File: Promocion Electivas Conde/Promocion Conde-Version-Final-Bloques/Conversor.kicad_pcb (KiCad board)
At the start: 4 copper layers, 0 parts

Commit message: Placa de prueba
Placa de 50 mm x 50 mm de 4 capas...
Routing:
- added copper zone on B.Cu, net (none)
- added copper zone on F.Cu, net (none)
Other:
- board outline added: 50 x 50 mm
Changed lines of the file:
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@@
   (general
     (thickness 1.6)
-    (drawings 0)
+    (drawings 4)
     (tracks 0)
     (zones 0)
@@
   (page A4)
   (layers
-    (0 GND power)
-    (1 12V power)
-    (2 3,3V power)
-    (31 Gnd power)
+    (0 F._GND power)
+    (1 F._12V power)
+    (2 B._3,3V power)
+    (31 B.Gnd power)
     (32 B.Adhes user)
     (33 F.Adhes user)
@@
     (uvia_drill 0.1)
   )
+  (gr_line (start 120 114) (end 120 64) (layer Edge.Cuts) (width 0.05))
+  (gr_line (start 170 114) (end 120 114) (layer Edge.Cuts) (width 0.05))
+  (gr_line (start 170 64) (end 170 114) (layer Edge.Cuts) (width 0.05))
+  (gr_line (start 120 64) (end 170 64) (layer Edge.Cuts) (width 0.05))
+  (zone (net 0) (net_name "") (layer F._GND) (hatch edge 0.508)
+    (connect_pads (clearance 0.508))
+    (min_thickness 0.254)
+    (fill yes (arc_segments 32) (thermal_gap 0.508) (thermal_bridge_width 0.508))
+    (polygon
+      (pts
+        (xy 170 114) (xy 120 114) (xy 120 64) (xy 170 64)
+      )
+    )
+  )
+  (zone (net 0) (net_name "") (layer B.Gnd) (hatch edge 0.508)
+    (connect_pads (clearance 0.508))
+    (min_thickness 0.254)
+    (fill yes (arc_segments 32) (thermal_gap 0.508) (thermal_bridge_width 0.508))
+    (polygon
+      (pts
+        (xy 170 114) (xy 120 114) (xy 120 64) (xy 170 64)
+      )
+    )
+  )
 )

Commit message: Creacion de las 4 capas...
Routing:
- added copper zone on B._3,3V, net (none)
- added copper zone on F._12V, net (none)
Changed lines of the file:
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@@
+    )
+  )
+  (zone (net 0) (net_name "") (layer F._12V) (hatch edge 0.508)
+    (connect_pads (clearance 0.508))
+    (min_thickness 0.254)
+    (fill yes (arc_segments 32) (thermal_gap 0.508) (thermal_bridge_width 0.508))
+    (polygon
+      (pts
+        (xy 170 114) (xy 120 114) (xy 120 64) (xy 170 64)
+      )
+    )
+  )
+  (zone (net 0) (net_name "") (layer B._3,3V) (hatch edge 0.508)
+    (connect_pads (clearance 0.508))
+    (min_thickness 0.254)
+    (fill yes (arc_segments 32) (thermal_gap 0.508) (thermal_bridge_width 0.508))
+    (polygon
+      (pts
+        (xy 170 114) (xy 120 114) (xy 120 64) (xy 170 64)
+      )
     )
   )

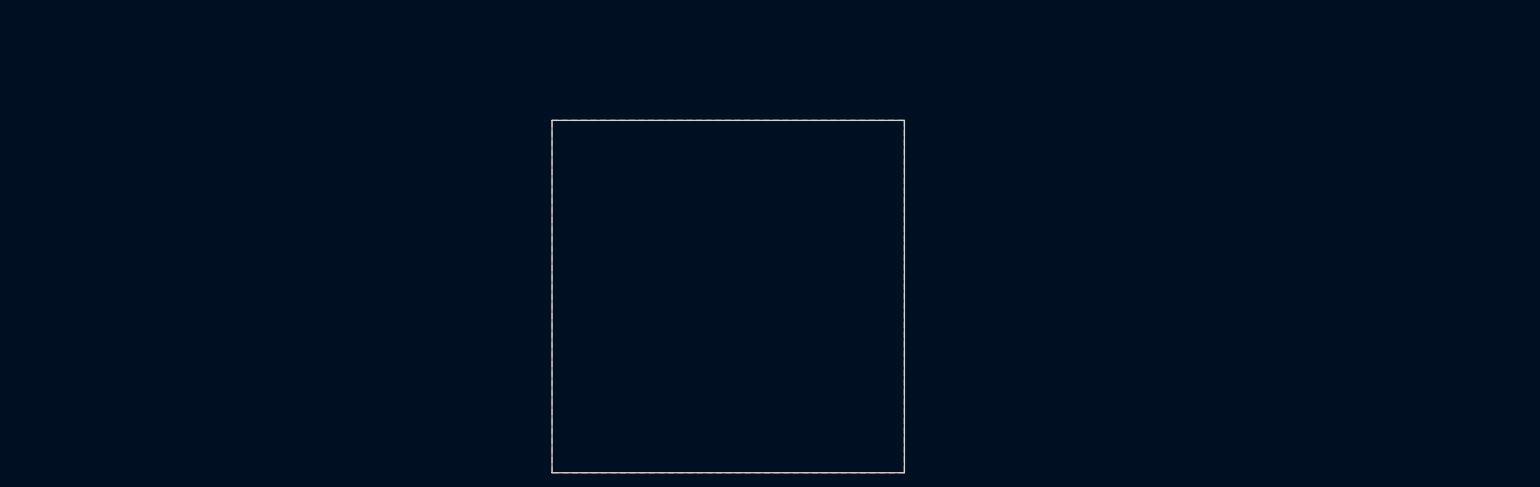
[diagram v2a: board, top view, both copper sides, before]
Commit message: Actualizacion
Actualizo los footprints del esquematico y se inicia el PCB
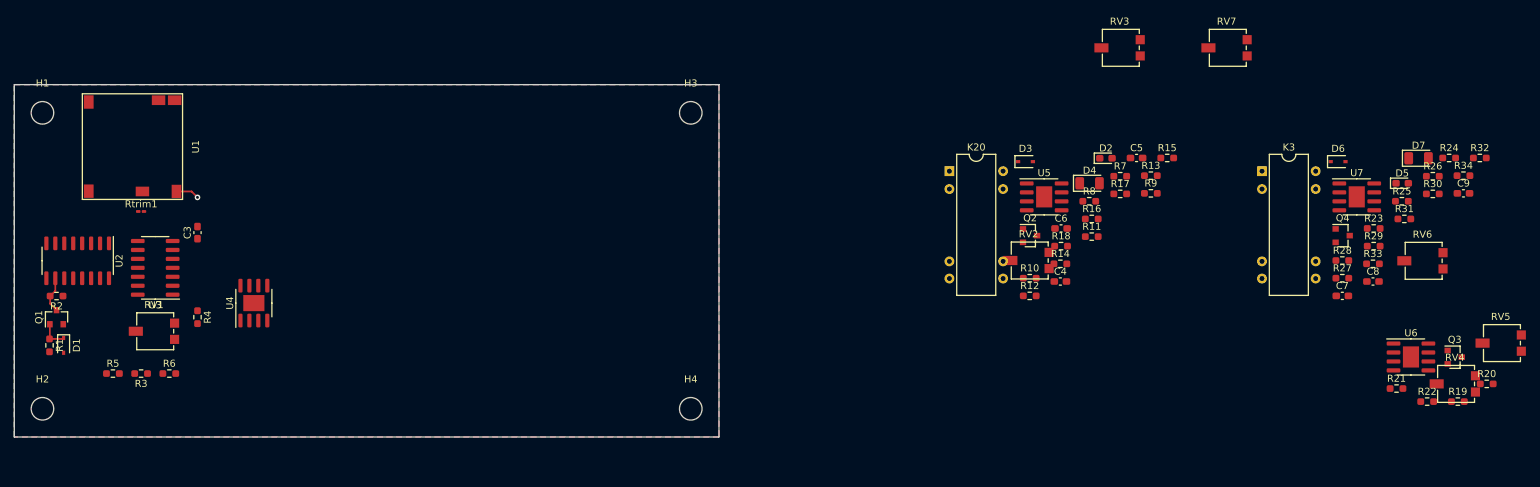
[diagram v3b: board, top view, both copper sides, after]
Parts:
- added C3: 0.022uF, Capacitor_SMD:C_0603_1608Metric_Pad1.08x0.95mm_HandSolder, F.Cu at (69.7, 79.9)
- added C4: 1uF, Capacitor_SMD:C_0603_1608Metric_Pad1.08x0.95mm_HandSolder, F.Cu at (192.1, 86.9)
- added C5: 1uF, Capacitor_SMD:C_0603_1608Metric_Pad1.08x0.95mm_HandSolder, F.Cu at (202.9, 69.3)
- added C6: 2.2uF, Capacitor_SMD:C_0603_1608Metric_Pad1.08x0.95mm_HandSolder, F.Cu at (192.2, 79.3)
- added C7: 1uF, Capacitor_SMD:C_0603_1608Metric_Pad1.08x0.95mm_HandSolder, F.Cu at (232.1, 88.9)
- added C8: 1uF, Capacitor_SMD:C_0603_1608Metric_Pad1.08x0.95mm_HandSolder, F.Cu at (236.5, 86.9)
- added C9: 2.2uF, Capacitor_SMD:C_0603_1608Metric_Pad1.08x0.95mm_HandSolder, F.Cu at (249.3, 74.4)
- added D1: 1N4148, Diode_SMD:D_SOD-323, F.Cu at (50.7, 95.9)
- added D2: FD300, Diode_SMD:D_0603_1608Metric_Pad1.05x0.95mm_HandSolder, F.Cu at (198.6, 69.4)
- added D3: 1N4148, Diode_SMD:D_SOD-323, F.Cu at (187.2, 69.9)
- added D4: LED, LED_SMD:LED_1206_3216Metric, F.Cu at (196.3, 72.9)
- added D5: FD300, Diode_SMD:D_0603_1608Metric_Pad1.05x0.95mm_HandSolder, F.Cu at (240.6, 72.9)
- added D6: 1N4148, Diode_SMD:D_SOD-323, F.Cu at (231.5, 69.9)
- added D7: LED, LED_SMD:LED_1206_3216Metric, F.Cu at (243.0, 69.4)
- added H1: MountingHole, MountingHole:MountingHole_3.2mm_M3, F.Cu at (47.7, 62.9)
- added H2: MountingHole, MountingHole:MountingHole_3.2mm_M3, F.Cu at (47.7, 104.9)
- added H3: MountingHole, MountingHole:MountingHole_3.2mm_M3, F.Cu at (139.7, 62.9)
- added H4: MountingHole, MountingHole:MountingHole_3.2mm_M3, F.Cu at (139.7, 104.9)
- added K20: DIPxx-1Cxx-51x, Relay_THT:Relay_StandexMeder_DIP_LowProfile, F.Cu at (176.4, 71.2)
- added K3: DIPxx-1Cxx-51x, Relay_THT:Relay_StandexMeder_DIP_LowProfile, F.Cu at (220.7, 71.2)
- added Q1: BC848, Package_TO_SOT_SMD:SOT-23, F.Cu at (49.7, 91.9)
- added Q2: BC848, Package_TO_SOT_SMD:SOT-23, F.Cu at (187.8, 80.4)
- added Q3: PN2222A, Package_TO_SOT_SMD:SOT-23, F.Cu at (248.1, 97.6)
- added Q4: BC848, Package_TO_SOT_SMD:SOT-23, F.Cu at (232.2, 80.4)
- added R1: 10K, Resistor_SMD:R_0603_1608Metric_Pad0.98x0.95mm_HandSolder, F.Cu at (48.7, 95.9)
- added R10: 10M, Resistor_SMD:R_0603_1608Metric_Pad0.98x0.95mm_HandSolder, F.Cu at (187.8, 86.4)
- added R11: 47K, Resistor_SMD:R_0603_1608Metric_Pad0.98x0.95mm_HandSolder, F.Cu at (196.6, 80.5)
- added R12: 68K, Resistor_SMD:R_0603_1608Metric_Pad0.98x0.95mm_HandSolder, F.Cu at (187.8, 88.9)
- added R13: 2.2M, Resistor_SMD:R_0603_1608Metric_Pad0.98x0.95mm_HandSolder, F.Cu at (205.0, 71.8)
- added R14: 10K, Resistor_SMD:R_0603_1608Metric_Pad0.98x0.95mm_HandSolder, F.Cu at (192.1, 84.4)
- added R15: 10M, Resistor_SMD:R_0603_1608Metric_Pad0.98x0.95mm_HandSolder, F.Cu at (207.3, 69.3)
- added R16: R, Resistor_SMD:R_0603_1608Metric_Pad0.98x0.95mm_HandSolder, F.Cu at (196.6, 78.0)
- added R17: R, Resistor_SMD:R_0603_1608Metric_Pad0.98x0.95mm_HandSolder, F.Cu at (200.6, 74.4)
- added R18: 6.8K, Resistor_SMD:R_0603_1608Metric_Pad0.98x0.95mm_HandSolder, F.Cu at (192.2, 81.8)
- added R19: 10k, Resistor_SMD:R_0603_1608Metric_Pad0.98x0.95mm_HandSolder, F.Cu at (248.5, 103.9)
- added R2: 100K, Resistor_SMD:R_0603_1608Metric_Pad0.98x0.95mm_HandSolder, F.Cu at (49.7, 88.9)
- added R20: R, Resistor_SMD:R_0603_1608Metric_Pad0.98x0.95mm_HandSolder, F.Cu at (252.6, 101.4)
- added R21: 1k, Resistor_SMD:R_0603_1608Metric_Pad0.98x0.95mm_HandSolder, F.Cu at (239.8, 102.1)
- added R22: 320, Resistor_SMD:R_0603_1608Metric_Pad0.98x0.95mm_HandSolder, F.Cu at (244.2, 103.9)
- added R23: 100K, Resistor_SMD:R_0603_1608Metric_Pad0.98x0.95mm_HandSolder, F.Cu at (236.6, 79.3)
- added R24: 100K, Resistor_SMD:R_0603_1608Metric_Pad0.98x0.95mm_HandSolder, F.Cu at (247.3, 69.3)
- added R25: 10K, Resistor_SMD:R_0603_1608Metric_Pad0.98x0.95mm_HandSolder, F.Cu at (240.6, 75.5)
- added R26: 10M, Resistor_SMD:R_0603_1608Metric_Pad0.98x0.95mm_HandSolder, F.Cu at (245.0, 71.9)
- added R27: 68K, Resistor_SMD:R_0603_1608Metric_Pad0.98x0.95mm_HandSolder, F.Cu at (232.1, 86.4)
- added R28: 47K, Resistor_SMD:R_0603_1608Metric_Pad0.98x0.95mm_HandSolder, F.Cu at (232.1, 83.9)
- added R29: 2.2M, Resistor_SMD:R_0603_1608Metric_Pad0.98x0.95mm_HandSolder, F.Cu at (236.6, 81.8)
- added R3: 100K, Resistor_SMD:R_0603_1608Metric_Pad0.98x0.95mm_HandSolder, F.Cu at (61.7, 99.9)
- added R30: 10K, Resistor_SMD:R_0603_1608Metric_Pad0.98x0.95mm_HandSolder, F.Cu at (245.0, 74.4)
- added R31: 10M, Resistor_SMD:R_0603_1608Metric_Pad0.98x0.95mm_HandSolder, F.Cu at (240.9, 78.0)
- added R32: R, Resistor_SMD:R_0603_1608Metric_Pad0.98x0.95mm_HandSolder, F.Cu at (251.7, 69.3)
- added R33: R, Resistor_SMD:R_0603_1608Metric_Pad0.98x0.95mm_HandSolder, F.Cu at (236.5, 84.4)
- added R34: 6.8K, Resistor_SMD:R_0603_1608Metric_Pad0.98x0.95mm_HandSolder, F.Cu at (249.3, 71.8)
- added R4: 100K, Resistor_SMD:R_0603_1608Metric_Pad0.98x0.95mm_HandSolder, F.Cu at (69.7, 91.9)
- added R5: 100K, Resistor_SMD:R_0603_1608Metric_Pad0.98x0.95mm_HandSolder, F.Cu at (57.7, 99.9)
- added R6: 100K, Resistor_SMD:R_0603_1608Metric_Pad0.98x0.95mm_HandSolder, F.Cu at (65.7, 99.9)
- added R7: 100K, Resistor_SMD:R_0603_1608Metric_Pad0.98x0.95mm_HandSolder, F.Cu at (200.6, 71.9)
- added R8: 100K, Resistor_SMD:R_0603_1608Metric_Pad0.98x0.95mm_HandSolder, F.Cu at (196.2, 75.5)
- added R9: 10K, Resistor_SMD:R_0603_1608Metric_Pad0.98x0.95mm_HandSolder, F.Cu at (205.0, 74.4)
- added RV1: 20K, Potentiometer_SMD:Potentiometer_Vishay_TS53YL_Vertical, F.Cu at (63.7, 93.9)
- added RV2: 10K, Potentiometer_SMD:Potentiometer_Vishay_TS53YL_Vertical, F.Cu at (187.8, 83.9)
- added RV3: R_POT, Potentiometer_SMD:Potentiometer_Vishay_TS53YL_Vertical, F.Cu at (200.7, 53.7)
- added RV4: 10k, Potentiometer_SMD:Potentiometer_Vishay_TS53YL_Vertical, F.Cu at (248.3, 101.4)
- added RV5: 10k, Potentiometer_SMD:Potentiometer_Vishay_TS53YL_Vertical, F.Cu at (254.8, 95.6)
- added RV6: 10K, Potentiometer_SMD:Potentiometer_Vishay_TS53YL_Vertical, F.Cu at (243.7, 83.9)
- added RV7: R_POT, Potentiometer_SMD:Potentiometer_Vishay_TS53YL_Vertical, F.Cu at (215.9, 53.7)
- added Rtrim1: R, Resistor_SMD:R_0201_0603Metric_Pad0.64x0.40mm_HandSolder, F.Cu at (61.7, 76.9)
- added U1: MTC1S2412MC-R13, Converter_DCDC:MTC1S2412MC-R13, F.Cu at (65.7, 63.9)
- added U2: 4040, Package_SO:SOIC-16_3.9x9.9mm_P1.27mm, F.Cu at (52.7, 83.9)
- added U3: 4070, Package_SO:SOIC-14_3.9x8.7mm_P1.27mm, F.Cu at (63.7, 84.9)
- added U4: TL082, Package_SO:SOIC-8-1EP_3.9x4.9mm_P1.27mm_EP2.29x3mm, F.Cu at (77.7, 89.9)
- added U5: TL082, Package_SO:SOIC-8-1EP_3.9x4.9mm_P1.27mm_EP2.29x3mm, F.Cu at (189.8, 74.9)
- added U6: TL082, Package_SO:SOIC-8-1EP_3.9x4.9mm_P1.27mm_EP2.29x3mm, F.Cu at (241.9, 97.6)
- added U7: TL082, Package_SO:SOIC-8-1EP_3.9x4.9mm_P1.27mm_EP2.29x3mm, F.Cu at (234.2, 74.9)
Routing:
- net Net-(Q1-Pad3): track 0.00 -> 5.21 mm
- net Net-(D1-Pad1): track 0.00 -> 4.17 mm
- net /Comparador_y_salida_relé_arranque/12V: track 0.00 -> 3.33 mm, vias 0 -> 1
- added copper zone on F._12V, net /Comparador_y_salida_relé_arranque/12V
- added copper zone on F.Cu, net GND
- removed copper zone on F.Cu, net (none)
- removed copper zone on F._12V, net (none)
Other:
- board size 50 x 50 mm -> 100 x 50 mm

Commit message: Ruteo, falta algunas pistas todavia...
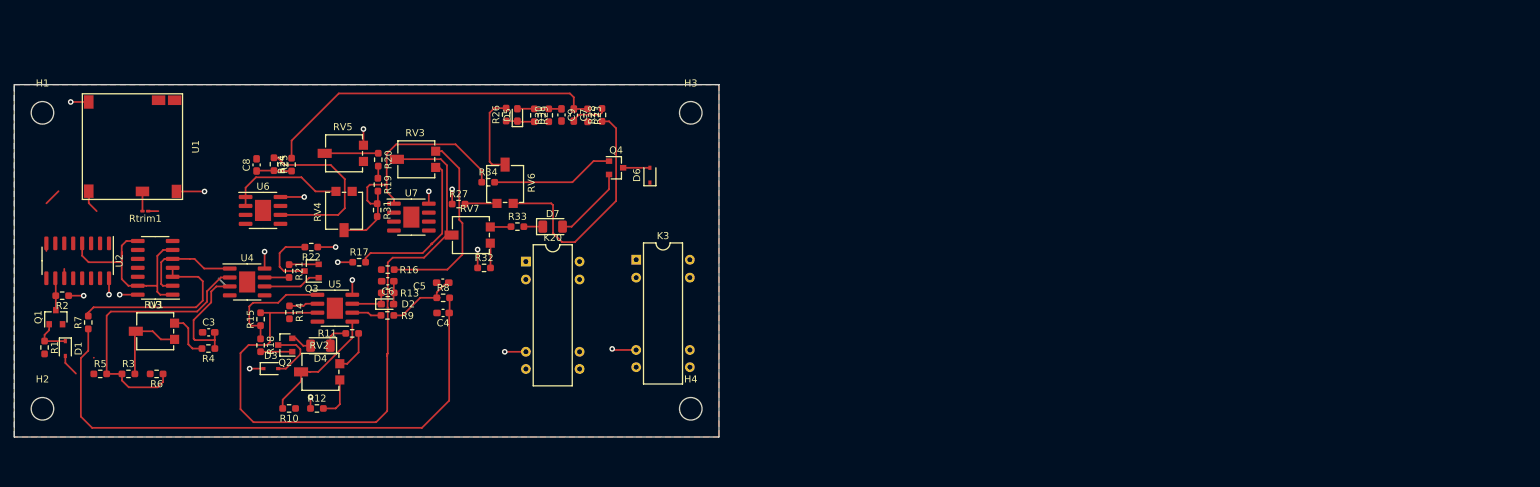
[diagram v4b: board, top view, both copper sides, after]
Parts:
- moved RV5 166.5 mm to (90.5, 68.7)
- moved R24 164.3 mm to (83.0, 70.3), turned to 90 degrees
- moved U6 164.2 mm to (79.0, 76.8)
- moved Q3 162.7 mm to (85.9, 85.4), turned to 180 degrees
- moved R20 160.5 mm to (95.3, 69.6), turned to 270 degrees
- moved R25 160.1 mm to (80.5, 70.2), turned to 270 degrees
- moved R22 159.9 mm to (85.8, 82.0), turned to 180 degrees
- moved RV4 159.7 mm to (90.5, 76.8), turned to 90 degrees
- moved C8 159.3 mm to (78.1, 70.3), turned to 90 degrees
- moved R21 158.0 mm to (82.7, 85.4), turned to 270 degrees
- moved R19 156.3 mm to (95.3, 73.1), turned to 270 degrees
- moved R7 147.9 mm to (54.2, 92.7), turned to 90 degrees
- moved R31 145.8 mm to (95.2, 76.7), turned to 270 degrees
- moved R32 142.2 mm to (110.4, 84.9)
- moved R34 138.4 mm to (110.9, 72.8)
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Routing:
- net /Comparador_y_salida_relé_arranque/24V: track 0.00 -> 108.6 mm, vias 0 -> 4
- net Net-(R15-Pad2): track 0.00 -> 96.1 mm
- net Net-(C4-Pad1): track 0.00 -> 82.0 mm
- net Net-(C7-Pad1): track 0.00 -> 49.1 mm
- net /Comparador_y_salida_relé_arranque/12V: track 3.33 -> 46.5 mm, vias 1 -> 14
- net Net-(R3-Pad1): track 0.00 -> 39.6 mm
- net Net-(R28-Pad1): track 0.00 -> 34.3 mm
- net Net-(U2-Pad4): track 0.00 -> 31.5 mm
- net Net-(R31-Pad1): track 0.00 -> 30.8 mm
- net Net-(R16-Pad1): track 0.00 -> 27.9 mm
- net /Comparador_y_salida_relé_arranque/A: track 0.00 -> 26.0 mm
- net GND: track 0.00 -> 25.1 mm
- net Net-(R25-Pad1): track 0.00 -> 25.0 mm
- net Net-(R17-Pad2): track 0.00 -> 23.1 mm
- net Net-(R10-Pad2): track 0.00 -> 17.8 mm
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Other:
- board text added: "Falta elegir footprint de los reles (K20 y K3)"

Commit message: Layers de 12V y 24V
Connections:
- net /Comparador_y_salida_relé_arranque/12V renamed +12V
- net /Comparador_y_salida_relé_arranque/24V renamed +24V
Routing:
- net /Comparador_y_salida_relé_arranque/12V: track 0.00 -> 1.41 mm
- net +12V: track 46.5 -> 45.1 mm
- added copper zone on B._24V, net +24V
- removed copper zone on B._3,3V, net (none)
